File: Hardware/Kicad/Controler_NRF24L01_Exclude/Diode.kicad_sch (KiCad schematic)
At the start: 40 parts, among them U4 PCA9685PW

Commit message: update of the folder 'controler_NRF24L01_Exclude' -> replace by the correction given
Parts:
- removed D3: D_Small, LED_SMD:LED_0603_1608Metric_Pad1.05x0.95mm_HandSolder, symbol Device:D_Small
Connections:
- net Glob_Alim: now also U4.28 (VDD)
- net at D16.2 (A): now also U4.18 (LED11); no longer U4.19 (LED12)
- net at D17.2 (A): now also U4.17 (LED10); no longer U4.20 (LED13)
- net at D13.2 (A): now also U4.21 (LED14); no longer U4.16 (LED9)
- net at D5.2 (A): now also U4.8 (LED2); no longer U4.7 (LED1)
- net at D19.2 (A): now also U4.15 (LED8); no longer U4.22 (LED15)
- net at D18.2 (A): now also U4.16 (LED9); no longer U4.21 (LED14)
- net at D12.2 (A): now also U4.22 (LED15); no longer U4.15 (LED8)
- net at D14.2 (A): now also U4.20 (LED13); no longer U4.17 (LED10)
- net at D15.2 (A): now also U4.19 (LED12); no longer U4.18 (LED11)
- net at U4.6 (LED0): now also D7.2 (A); no longer D4.2 (A)
- net at D6.2 (A): now also U4.7 (LED1); no longer U4.8 (LED2)
- net at U4.9 (LED3): now also D4.2 (A); no longer D7.2 (A)
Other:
- moved on the sheet: D12, D13, D14, D15, D16, D17, D18, D19, D4, D5, D6, D7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

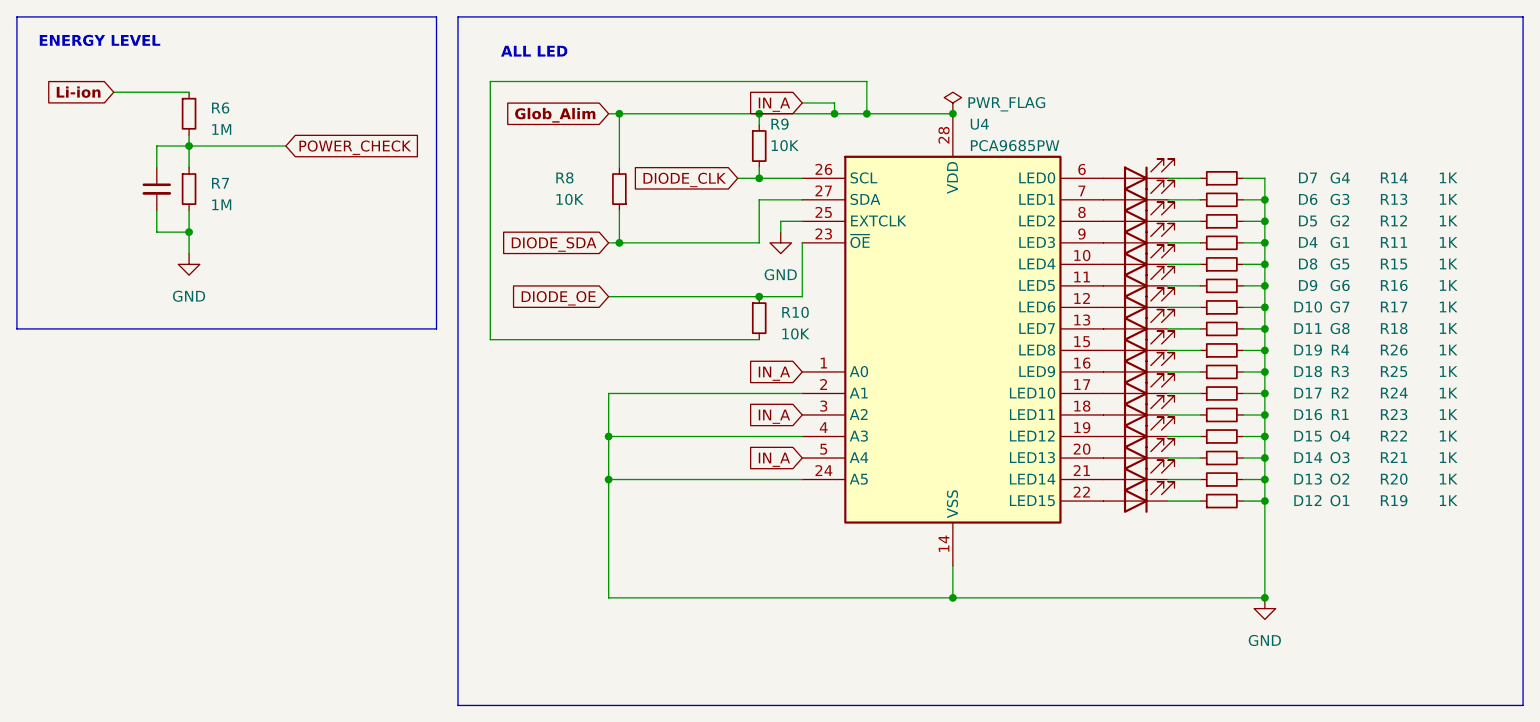
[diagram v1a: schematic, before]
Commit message: Update v2.2a - Plug_NRF24L01_Exclude (SWD_Connector, GND Vias) - Controller_NRF24L01_Exclude (Schematic) - Cleaned Folders
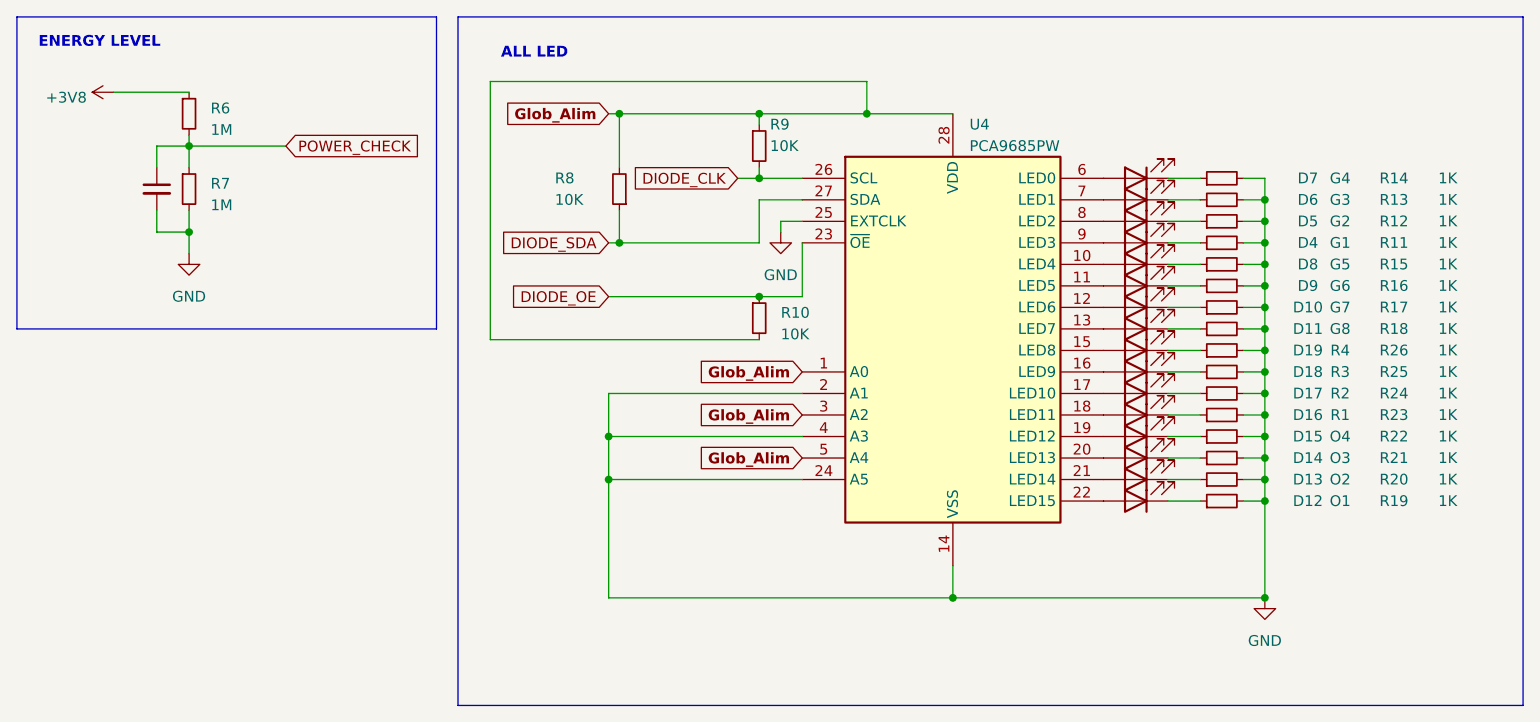
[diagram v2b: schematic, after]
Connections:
- net Li-ion renamed +3V8
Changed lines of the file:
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@@
   (junction (at 251.46 39.37) (diameter 0) (color 0 0 0 0)
   )
-  (junction (at 214.63 26.67) (diameter 0) (color 0 0 0 0)
-  )
   (junction (at 251.46 46.99) (diameter 0) (color 0 0 0 0)
   )
@@
   (junction (at 251.46 72.39) (diameter 0) (color 0 0 0 0)
   )
-  (junction (at 200.66 26.67) (diameter 0) (color 0 0 0 0)
-  )
   (junction (at 251.46 57.15) (diameter 0) (color 0 0 0 0)
   )
@@
     (stroke (width 0) (type default))
   )
-  (wire (pts (xy 200.66 26.67) (xy 191.77 26.67))
+  (wire (pts (xy 191.77 26.67) (xy 204.47 26.67))
     (stroke (width 0) (type default))
   )
@@
     (stroke (width 0) (type default))
   )
-  (wire (pts (xy 204.47 26.67) (xy 200.66 26.67))
-    (stroke (width 0) (type default))
-  )
   (polyline (pts (xy 281.94 15.24) (xy 281.94 96.52))
     (stroke (width 0) (type default))
@@
     (stroke (width 0) (type default))
   )
-  (wire (pts (xy 196.85 25.4) (xy 200.66 25.4))
-    (stroke (width 0) (type default))
-  )
   (wire (pts (xy 173.99 48.26) (xy 191.77 48.26))
     (stroke (width 0) (type default))
@@
   )
   (wire (pts (xy 248.92 57.15) (xy 251.46 57.15))
-    (stroke (width 0) (type default))
-  )
-  (wire (pts (xy 200.66 25.4) (xy 200.66 26.67))
     (stroke (width 0) (type default))
   )
@@
     (effects (font (size 1.27 1.27) (thickness 0.254) bold) (justify left bottom))
   )
-  (global_label "IN_A" (shape input) (at 196.85 62.23 180) (fields_autoplaced)
-    (effects (font (size 1.27 1.27)) (justify right))
-    (property "Intersheetrefs" "${INTERSHEET_REFS}" (at 189.9527 62.23 0)
+  (global_label "Glob_Alim" (shape input) (at 196.85 57.15 180) (fields_autoplaced)
+    (effects (font (size 1.27 1.27) bold) (justify right))
+    (property "Intersheetrefs" "${INTERSHEET_REFS}" (at 184.2631 57.15 0)
       (effects (font (size 1.27 1.27)) (justify right) hide)
     )
@@
     )
   )
-  (global_label "Li-ion" (shape input) (at 115.57 24.13 180) (fields_autoplaced)
-    (effects (font (size 1.27 1.27) bold) (justify right))
-    (property "Intersheetrefs" "${INTERSHEET_REFS}" (at 106.1277 24.13 0)
-      (effects (font (size 1.27 1.27)) (justify right) hide)
-    )
-  )
   (global_label "DIODE_CLK" (shape input) (at 189.23 34.29 180) (fields_autoplaced)
     (effects (font (size 1.27 1.27)) (justify right))
@@
     )
   )
-  (global_label "IN_A" (shape input) (at 196.85 25.4 180) (fields_autoplaced)
-    (effects (font (size 1.27 1.27)) (justify right))
-    (property "Intersheetrefs" "${INTERSHEET_REFS}" (at 189.9527 25.4 0)
-      (effects (font (size 1.27 1.27)) (justify right) hide)
-    )
-  )
   (global_label "DIODE_SDA" (shape input) (at 173.99 41.91 180) (fields_autoplaced)
     (effects (font (size 1.27 1.27)) (justify right))
@@
     )
   )
+  (global_label "Glob_Alim" (shape input) (at 196.85 62.23 180) (fields_autoplaced)
+    (effects (font (size 1.27 1.27) bold) (justify right))
+    (property "Intersheetrefs" "${INTERSHEET_REFS}" (at 184.2631 62.23 0)
+      (effects (font (size 1.27 1.27)) (justify right) hide)
+    )
+  )
   (global_label "POWER_CHECK" (shape input) (at 135.89 30.48 0) (fields_autoplaced)
     (effects (font (size 1.27 1.27)) (justify left))
@@
     )
   )
-  (global_label "IN_A" (shape input) (at 196.85 57.15 180) (fields_autoplaced)
-    (effects (font (size 1.27 1.27)) (justify right))
-    (property "Intersheetrefs" "${INTERSHEET_REFS}" (at 189.9527 57.15 0)
+  (global_label "Glob_Alim" (shape input) (at 196.85 67.31 180) (fields_autoplaced)
+    (effects (font (size 1.27 1.27) bold) (justify right))
+    (property "Intersheetrefs" "${INTERSHEET_REFS}" (at 184.2631 67.31 0)
       (effects (font (size 1.27 1.27)) (justify right) hide)
-    )
-  )
-  (global_label "IN_A" (shape input) (at 196.85 67.31 180) (fields_autoplaced)
-    (effects (font (size 1.27 1.27)) (justify right))
-    (property "Intersheetrefs" "${INTERSHEET_REFS}" (at 189.9527 67.31 0)
-      (effects (font (size 1.27 1.27)) (justify right) hide)
-    )
-  )
-  (symbol (lib_id "power:PWR_FLAG") (at 214.63 26.67 0) (unit 1)
-    (in_bom yes) (on_board yes) (dnp no)
-    (property "Reference" "#FLG06" (at 214.63 24.765 0)
-      (effects (font (size 1.27 1.27)) hide)
-    )
-    (property "Value" "PWR_FLAG" (at 220.98 25.4 0)
-      (effects (font (size 1.27 1.27)))
-    )
-    (property "Footprint" "" (at 214.63 26.67 0)
-      (effects (font (size 1.27 1.27)) hide)
-    )
-    (property "Datasheet" "~" (at 214.63 26.67 0)
-      (effects (font (size 1.27 1.27)) hide)
-    )
-    (pin "1")
-    (instances
-      (project "Controller_NRF24L01_Include"
-        (path "/700f508b-c905-4d29-9c95-836d8db731fc/efd5fe6b-cfb4-4a93-a48a-8f57d2a0a889"
-          (reference "#FLG06") (unit 1)
-        )
-      )
-      (project "Controler_NRF24L01_Exclude"
-        (path "/76ef48f1-60b7-4c4b-a0ce-73b6af33b115/afa1107b-0419-432b-b3a6-c7617e352999"
-          (reference "#FLG06") (unit 1)
-        )
-      )
     )
   )
@@
         )
       )
+    )
+  )
+  (symbol (lib_id "power:+3V8") (at 115.57 24.13 90) (unit 1)
+    (in_bom yes) (on_board yes) (dnp no) (fields_autoplaced)
+    (property "Reference" "#PWR021" (at 119.38 24.13 0)
+      (effects (font (size 1.27 1.27)) hide)
+    )
+    (property "Value" "+3V8" (at 112.395 24.765 90)
+      (effects (font (size 1.27 1.27)) (justify left))
+    )
+    (property "Footprint" "" (at 115.57 24.13 0)
+      (effects (font (size 1.27 1.27)) hide)
+    )
+    (property "Datasheet" "" (at 115.57 24.13 0)
+      (effects (font (size 1.27 1.27)) hide)
+    )
+    (pin "1")
+    (instances
+      (project "Controler_NRF24L01_Exclude"
+        (path "/76ef48f1-60b7-4c4b-a0ce-73b6af33b115"
+          (reference "#PWR021") (unit 1)
+        )
+        (path "/76ef48f1-60b7-4c4b-a0ce-73b6af33b115/afa1107b-0419-432b-b3a6-c7617e352999"
+          (reference "#PWR010") (unit 1)
+        )
+      )
